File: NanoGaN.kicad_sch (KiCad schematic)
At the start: 20 parts, among them J1 XT60-M, J2 XT60-M, J3 Phase_U, J4 Phase_V, J5 Phase_W

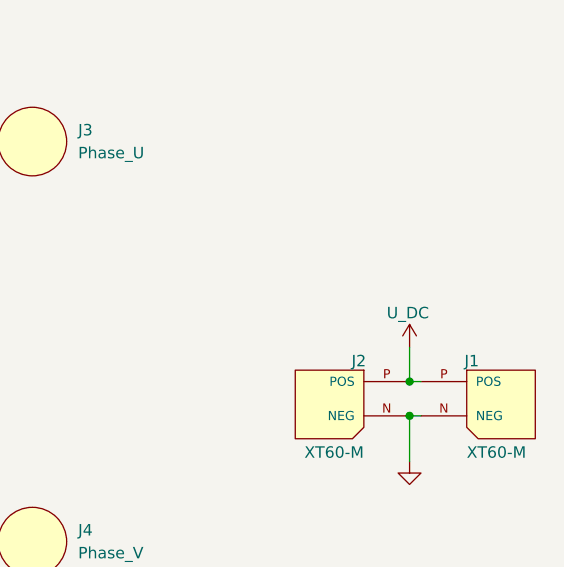
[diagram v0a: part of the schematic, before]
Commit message: various silk screen changes
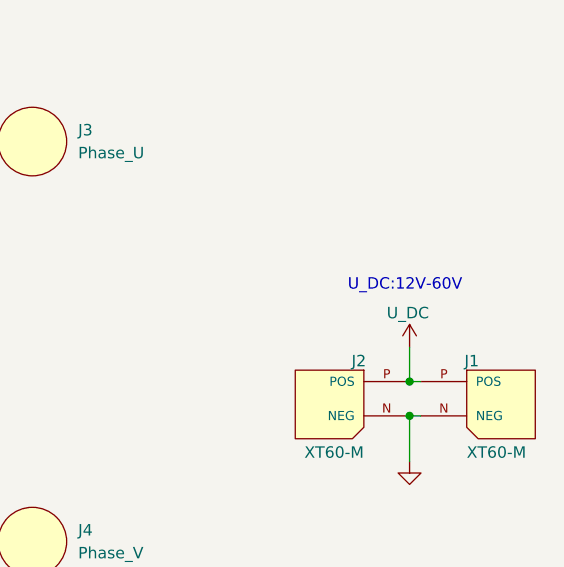
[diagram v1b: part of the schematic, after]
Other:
- note added: "U_DC:12V-60V"
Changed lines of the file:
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@@
+		)
+	)
+	(text "U_DC:12V-60V"
+		(exclude_from_sim no)
+		(at 247.142 56.642 0)
+		(effects
+			(font
+				(size 1.27 1.27)
+			)
 		)
 	)

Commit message: schematic and PCB reviews are done, ready for release and first order.
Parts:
- removed J3: Phase_U, TerminalBlock_Wuerth:Wuerth_REDCUBE-THR_WP-THRBU_74650073_THR, symbol NanoGaN:Power_Welding_PAD
- removed J4: Phase_V, TerminalBlock_Wuerth:Wuerth_REDCUBE-THR_WP-THRBU_74650073_THR, symbol NanoGaN:Power_Welding_PAD
- removed J5: Phase_W, TerminalBlock_Wuerth:Wuerth_REDCUBE-THR_WP-THRBU_74650073_THR, symbol NanoGaN:Power_Welding_PAD
- added J3, J4, J5: Phase_U, TerminalBlock_Wuerth:Wuerth_REDCUBE-THR_WP-THRBU_74650073_THR, symbol Connector:Screw_Terminal_01x01
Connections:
- net HalfBridgeU/PHASE: now also J3.1 (Pin_1)
- net HalfBridgeV/PHASE: now also J4.1 (Pin_1)
- net HalfBridgeW/PHASE: now also J5.1 (Pin_1)
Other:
- company: ErenAkbayin -> Eren Akbayin
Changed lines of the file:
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@@
 	(title_block
 		(title "NanoGaN")
-		(date "2026-01-16")
-		(rev "A")
-		(company "ErenAkbayin")
+		(date "2026-02-22")
+		(rev "A01")
+		(company "Eren Akbayin")
 	)
 	(rectangle
@@
 	(wire
 		(pts
-			(xy 189.23 40.64) (xy 194.31 40.64)
+			(xy 189.23 40.64) (xy 196.85 40.64)
 		)
 		(stroke
@@
 	(wire
 		(pts
-			(xy 189.23 85.09) (xy 194.31 85.09)
+			(xy 189.23 85.09) (xy 196.85 85.09)
 		)
 		(stroke
@@
 	(wire
 		(pts
-			(xy 189.23 129.54) (xy 193.04 129.54)
+			(xy 189.23 129.54) (xy 196.85 129.54)
 		)
 		(stroke
@@
 				(path "/aa8a494f-605e-4a00-9d3c-daec94709fcb"
 					(reference "FM2")
-					(unit 1)
-				)
-			)
-		)
-	)
-	(symbol
-		(lib_id "NanoGaN:Power_Welding_PAD")
-		(at 205.74 40.64 0)
-		(unit 1)
-		(exclude_from_sim no)
-		(in_bom yes)
-		(on_board yes)
-		(dnp no)
-		(fields_autoplaced yes)
-		(property "Reference" "J3"
-			(at 210.82 39.3699 0)
-			(effects
-				(font
-					(size 1.27 1.27)
-				)
-				(justify left)
-			)
-		)
-		(property "Value" "Phase_U"
-			(at 210.82 41.9099 0)
-			(effects
-				(font
-					(size 1.27 1.27)
-				)
-				(justify left)
-			)
-		)
-		(property "Footprint" "TerminalBlock_Wuerth:Wuerth_REDCUBE-THR_WP-THRBU_74650073_THR"
-			(at 205.74 40.64 0)
-			(effects
-				(font
-					(size 1.27 1.27)
-				)
-				(hide yes)
-			)
-		)
-		(property "Datasheet" ""
-			(at 205.74 40.64 0)
-			(effects
-				(font
-					(size 1.27 1.27)
-				)
-				(hide yes)
-			)
-		)
-		(property "Description" ""
-			(at 205.74 40.64 0)
-			(effects
-				(font
-					(size 1.27 1.27)
-				)
-			)
-		)
-		(pin "1"
-		)
-		(instances
-			(project ""
-				(path "/aa8a494f-605e-4a00-9d3c-daec94709fcb"
-					(reference "J3")
 					(unit 1)
 				)
@@
 	)
 	(symbol
-		(lib_id "NanoGaN:Power_Welding_PAD")
-		(at 204.47 129.54 0)
-		(unit 1)
-		(exclude_from_sim no)
-		(in_bom yes)
-		(on_board yes)
-		(dnp no)
-		(fields_autoplaced yes)
-		(property "Reference" "J5"
-			(at 209.55 128.2699 0)
-			(effects
-				(font
-					(size 1.27 1.27)
-				)
-				(justify left)
-			)
-		)
-		(property "Value" "Phase_W"
-			(at 209.55 130.8099 0)
-			(effects
-				(font
-					(size 1.27 1.27)
-				)
-				(justify left)
-			)
-		)
-		(property "Footprint" "TerminalBlock_Wuerth:Wuerth_REDCUBE-THR_WP-THRBU_74650073_THR"
-			(at 204.47 129.54 0)
-			(effects
-				(font
-					(size 1.27 1.27)
-				)
-				(hide yes)
-			)
-		)
-		(property "Datasheet" ""
-			(at 204.47 129.54 0)
-			(effects
-				(font
-					(size 1.27 1.27)
-				)
-				(hide yes)
-			)
-		)
-		(property "Description" ""
-			(at 204.47 129.54 0)
-			(effects
-				(font
-					(size 1.27 1.27)
-				)
-			)
-		)
-		(pin "1"
-		)
-		(instances
-			(project "NanoGaN"
-				(path "/aa8a494f-605e-4a00-9d3c-daec94709fcb"
-					(reference "J5")
-					(unit 1)
-				)
-			)
-		)
-	)
-	(symbol
 		(lib_name "MountingHole_Pad_3")
 		(lib_id "Mechanical:MountingHole_Pad")
@@
 	)
 	(symbol
+		(lib_id "Connector:Screw_Terminal_01x01")
+		(at 201.93 40.64 0)
+		(unit 1)
+		(exclude_from_sim no)
+		(in_bom yes)
+		(on_board yes)
+		(dnp no)
+		(fields_autoplaced yes)
+		(property "Reference" "J3"
+			(at 204.47 39.3699 0)
+			(effects
+				(font
+					(size 1.27 1.27)
+				)
+				(justify left)
+			)
+		)
+		(property "Value" "Phase_U"
+			(at 204.47 41.9099 0)
+			(effects
+				(font
+					(size 1.27 1.27)
+				)
+				(justify left)
+			)
+		)
+		(property "Footprint" "TerminalBlock_Wuerth:Wuerth_REDCUBE-THR_WP-THRBU_74650073_THR"
+			(at 201.93 40.64 0)
+			(effects
+				(font
+					(size 1.27 1.27)
+				)
+				(hide yes)
+			)
+		)
+		(property "Datasheet" ""
+			(at 201.93 40.64 0)
+			(effects
+				(font
+					(size 1.27 1.27)
+				)
+				(hide yes)
+			)
+		)
+		(property "Description" ""
+			(at 201.93 40.64 0)
+			(effects
+				(font
+					(size 1.27 1.27)
+				)
+			)
+		)
+		(pin "1"
+		)
+		(instances
+			(project ""
+				(path "/aa8a494f-605e-4a00-9d3c-daec94709fcb"
+					(reference "J3")
+					(unit 1)
+				)
+			)
+		)
+	)
+	(symbol
 		(lib_id "NanoGaN:XT60-M")
 		(at 242.57 66.04 0)
@@
 				(path "/aa8a494f-605e-4a00-9d3c-daec94709fcb"
 					(reference "J2")
-					(unit 1)
-				)
-			)
-		)
-	)
-	(symbol
-		(lib_id "NanoGaN:Power_Welding_PAD")
-		(at 205.74 85.09 0)
-		(unit 1)
-		(exclude_from_sim no)
-		(in_bom yes)
-		(on_board yes)
-		(dnp no)
-		(fields_autoplaced yes)
-		(property "Reference" "J4"
-			(at 210.82 83.8199 0)
-			(effects
-				(font
-					(size 1.27 1.27)
-				)
-				(justify left)
-			)
-		)
-		(property "Value" "Phase_V"
-			(at 210.82 86.3599 0)
-			(effects
-				(font
-					(size 1.27 1.27)
-				)
-				(justify left)
-			)
-		)
-		(property "Footprint" "TerminalBlock_Wuerth:Wuerth_REDCUBE-THR_WP-THRBU_74650073_THR"
-			(at 205.74 85.09 0)
-			(effects
-				(font
-					(size 1.27 1.27)
-				)
-				(hide yes)
-			)
-		)
-		(property "Datasheet" ""
-			(at 205.74 85.09 0)
-			(effects
-				(font
-					(size 1.27 1.27)
-				)
-				(hide yes)
-			)
-		)
-		(property "Description" ""
-			(at 205.74 85.09 0)
-			(effects
-				(font
-					(size 1.27 1.27)
-				)
-			)
-		)
-		(pin "1"
-		)
-		(instances
-			(project ""
-				(path "/aa8a494f-605e-4a00-9d3c-daec94709fcb"
-					(reference "J4")
 					(unit 1)
 				)
@@
 	)
 	(symbol
+		(lib_id "Connector:Screw_Terminal_01x01")
+		(at 201.93 129.54 0)
+		(unit 1)
+		(exclude_from_sim no)
+		(in_bom yes)
+		(on_board yes)
+		(dnp no)
+		(fields_autoplaced yes)
+		(property "Reference" "J5"
+			(at 204.47 128.2699 0)
+			(effects
+				(font
+					(size 1.27 1.27)
+				)
+				(justify left)
+			)
+		)
+		(property "Value" "Phase_U"
+			(at 204.47 130.8099 0)
+			(effects
+				(font
+					(size 1.27 1.27)
+				)
+				(justify left)
+			)
+		)
+		(property "Footprint" "TerminalBlock_Wuerth:Wuerth_REDCUBE-THR_WP-THRBU_74650073_THR"
+			(at 201.93 129.54 0)
+			(effects
+				(font
+					(size 1.27 1.27)
+				)
+				(hide yes)
+			)
+		)
+		(property "Datasheet" ""
+			(at 201.93 129.54 0)
+			(effects
+				(font
+					(size 1.27 1.27)
+				)
+				(hide yes)
+			)
+		)
+		(property "Description" ""
+			(at 201.93 129.54 0)
+			(effects
+				(font
+					(size 1.27 1.27)
+				)
+			)
+		)
+		(pin "1"
+		)
+		(instances
+			(project "NanoGaN"
+				(path "/aa8a494f-605e-4a00-9d3c-daec94709fcb"
+					(reference "J5")
+					(unit 1)
+				)
+			)
+		)
+	)
+	(symbol
 		(lib_name "MountingHole_Pad_8")
 		(lib_id "Mechanical:MountingHole_Pad")
@@
 					(unit 1)
 				)
+			)
+		)
+	)
+	(symbol
+		(lib_id "Connector:Screw_Terminal_01x01")
+		(at 201.93 85.09 0)
+		(unit 1)
+		(exclude_from_sim no)
+		(in_bom yes)
+		(on_board yes)
+		(dnp no)
+		(fields_autoplaced yes)
+		(property "Reference" "J4"
+			(at 204.47 83.8199 0)
+			(effects
+				(font
+					(size 1.27 1.27)
+				)
+				(justify left)
+			)
+		)
+		(property "Value" "Phase_U"
+			(at 204.47 86.3599 0)
+			(effects
+				(font
+					(size 1.27 1.27)
+				)
+				(justify left)
+			)
+		)
+		(property "Footprint" "TerminalBlock_Wuerth:Wuerth_REDCUBE-THR_WP-THRBU_74650073_THR"
+			(at 201.93 85.09 0)
+			(effects
+				(font
+					(size 1.27 1.27)
+				)
+				(hide yes)
+			)
+		)
+		(property "Datasheet" ""
+			(at 201.93 85.09 0)
+			(effects
+				(font
+					(size 1.27 1.27)
+				)
+				(hide yes)
+			)
+		)
+		(property "Description" ""
+			(at 201.93 85.09 0)
+			(effects
+				(font
+					(size 1.27 1.27)
+				)
+			)
+		)
+		(pin "1"
+		)
+		(instances
+			(project "NanoGaN"
+				(path "/aa8a494f-605e-4a00-9d3c-daec94709fcb"
+					(reference "J4")
+					(unit 1)
+				)

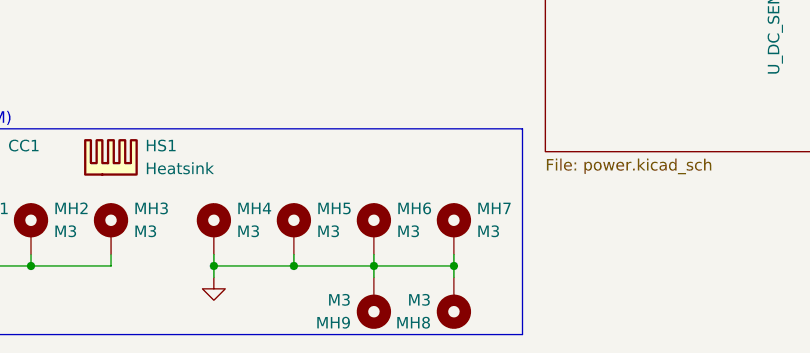
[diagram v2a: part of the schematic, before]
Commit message: gate driver change is complete
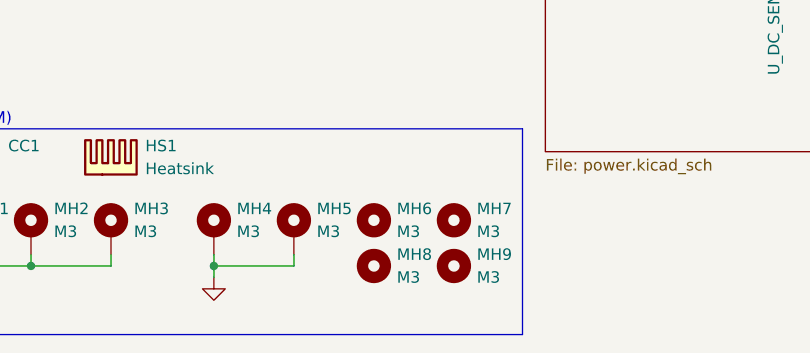
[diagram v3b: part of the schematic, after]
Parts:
- removed MH6, MH7, MH8, MH9: M3, MountingHole:MountingHole_3.2mm_M3_Pad_Via, symbol Mechanical:MountingHole_Pad
- added MH6, MH7, MH8, MH9: M3, MountingHole:MountingHole_3.2mm_M3, symbol Mechanical:MountingHole
